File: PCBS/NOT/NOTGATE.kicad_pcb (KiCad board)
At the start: 2 copper layers, 29 x 14 mm, 11 parts, among them J1 Conn_01x01_Socket, J3 Conn_01x03_Socket, U1 SN74LVC1GU04

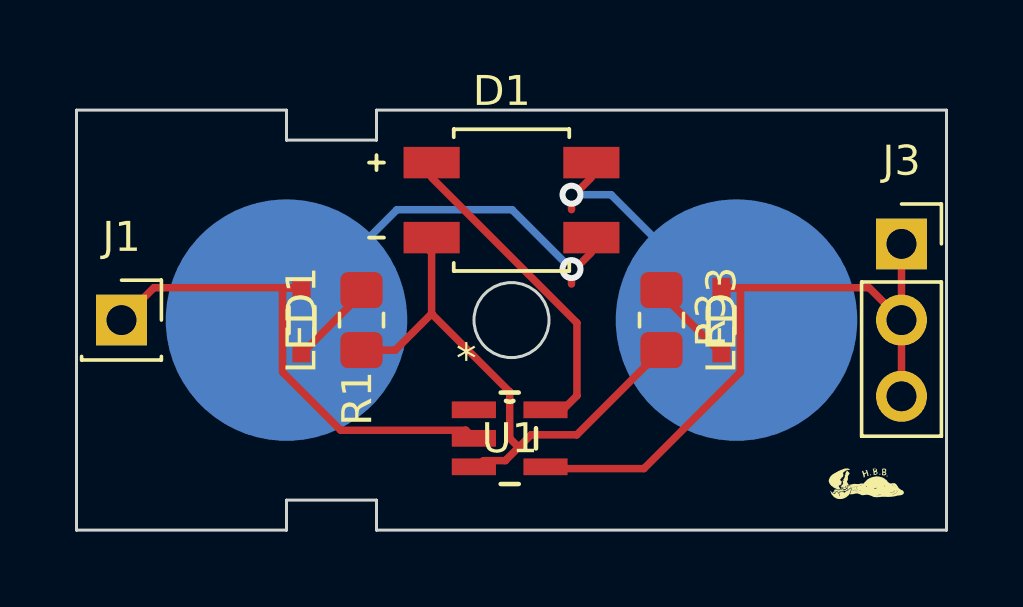
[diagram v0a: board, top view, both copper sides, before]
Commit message: Finished input PCB and fixed mux and not
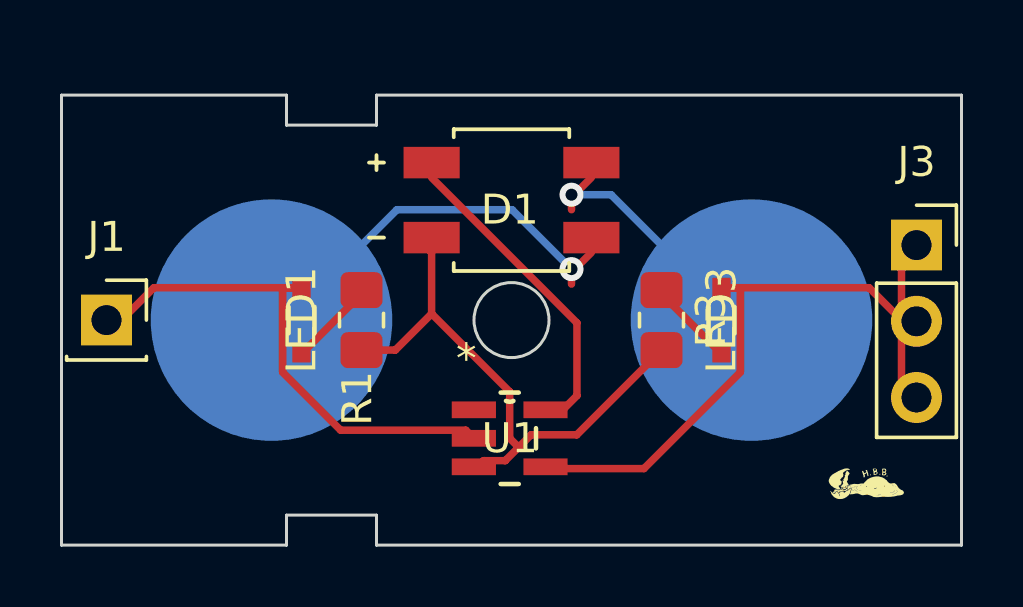
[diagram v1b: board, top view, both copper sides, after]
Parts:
- moved J3 0.50 mm to (168.5, 85.0)
- moved J1 0.50 mm to (141.5, 87.5)
- moved J4 0.50 mm to (147.0, 87.5)
- moved J5 0.50 mm to (163.0, 87.5)
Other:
- board size 29 x 14 mm -> 30 x 15 mm
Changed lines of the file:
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@@
   )
   (footprint "Connector_PinSocket_2.54mm:PinSocket_1x01_P2.54mm_Vertical" (layer "F.Cu")
-    (at 142 87.5)
+    (at 141.5 87.5)
     (descr "Through hole straight socket strip, 1x01, 2.54mm pitch, single row (from Kicad 4.0.7), script generated")
     (tags "Through hole socket strip THT 1x01 2.54mm single row")
@@
   )
   (footprint "Connector_PinSocket_2.54mm:PinSocket_1x03_P2.54mm_Vertical" (layer "F.Cu")
-    (at 168 84.96)
+    (at 168.5 85)
     (descr "Through hole straight socket strip, 1x03, 2.54mm pitch, single row (from Kicad 4.0.7), script generated")
     (tags "Through hole socket strip THT 1x03 2.54mm single row")
@@
     (property "SnapEDA_Link" "https://www.snapeda.com/parts/MB10F-13/Zetex/view-part/?ref=snap")
     (attr smd)
-    (fp_text reference "D1" (at -0.325 -3.635) (layer "F.SilkS")
+    (fp_text reference "D1" (at -0.06 0.32) (layer "F.SilkS")
         (effects (font (size 1 1) (thickness 0.15)))
     )
@@
   )
   (footprint "DigitalLogicFootprints:8mm-snap" (layer "B.Cu")
-    (at 147.5 87.5 180)
+    (at 147 87.5 180)
     (property "Sheetfile" "NOTGATE.kicad_sch")
     (property "Sheetname" "")
@@
   )
   (footprint "DigitalLogicFootprints:8mm-snap" (layer "B.Cu")
-    (at 162.5 87.5 180)
+    (at 163 87.5 180)
     (property "Sheetfile" "NOTGATE.kicad_sch")
     (property "Sheetname" "")
@@
       (net 7 "Net-(J5-PWR)") (pinfunction "PWR") (pintype "output"))
   )
+  (gr_circle (center 165.1 81.28) (end 165.1 81.28)
+    (stroke (width 0.1) (type default)) (fill none) (layer "Edge.Cuts"))
   (gr_poly
     (pts
-      (xy 140.5 80.5)
-      (xy 147.5 80.5)
-      (xy 147.5 81.5)
-      (xy 150.5 81.5)
-      (xy 150.5 80.5)
-      (xy 169.5 80.5)
-      (xy 169.5 94.5)
-      (xy 150.5 94.5)
-      (xy 150.5 93.5)
-      (xy 147.5 93.5)
-      (xy 147.5 94.5)
-      (xy 140.5 94.5)
+      (xy 140 95)
+      (xy 147.5 95)
+      (xy 147.5 94)
+      (xy 150.5 94)
+      (xy 150.5 95)
+      (xy 170 95)
+      (xy 170 80)
+      (xy 150.5 80)
+      (xy 150.5 81)
+      (xy 147.5 81)
+      (xy 147.5 80)
+      (xy 140 80)
     )
     (stroke (width 0.1) (type solid)) (fill none) (layer "Edge.Cuts"))
-  (gr_circle (center 165.1 81.28) (end 165.1 81.28)
-    (stroke (width 0.1) (type default)) (fill none) (layer "Edge.Cuts"))
   (gr_circle (center 155 87.5) (end 156.25 87.5)
     (stroke (width 0.1) (type default)) (fill none) (layer "Edge.Cuts"))
